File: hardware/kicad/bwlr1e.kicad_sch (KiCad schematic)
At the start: 62 parts, among them J1 Qwiic, Q1 AO3407, Q2 DMG1012UW, SW3 RESET, SW4 BOOT, U1 BME688, U2 RAK3172, U3 AEM10941-QFN, U4 XC6215

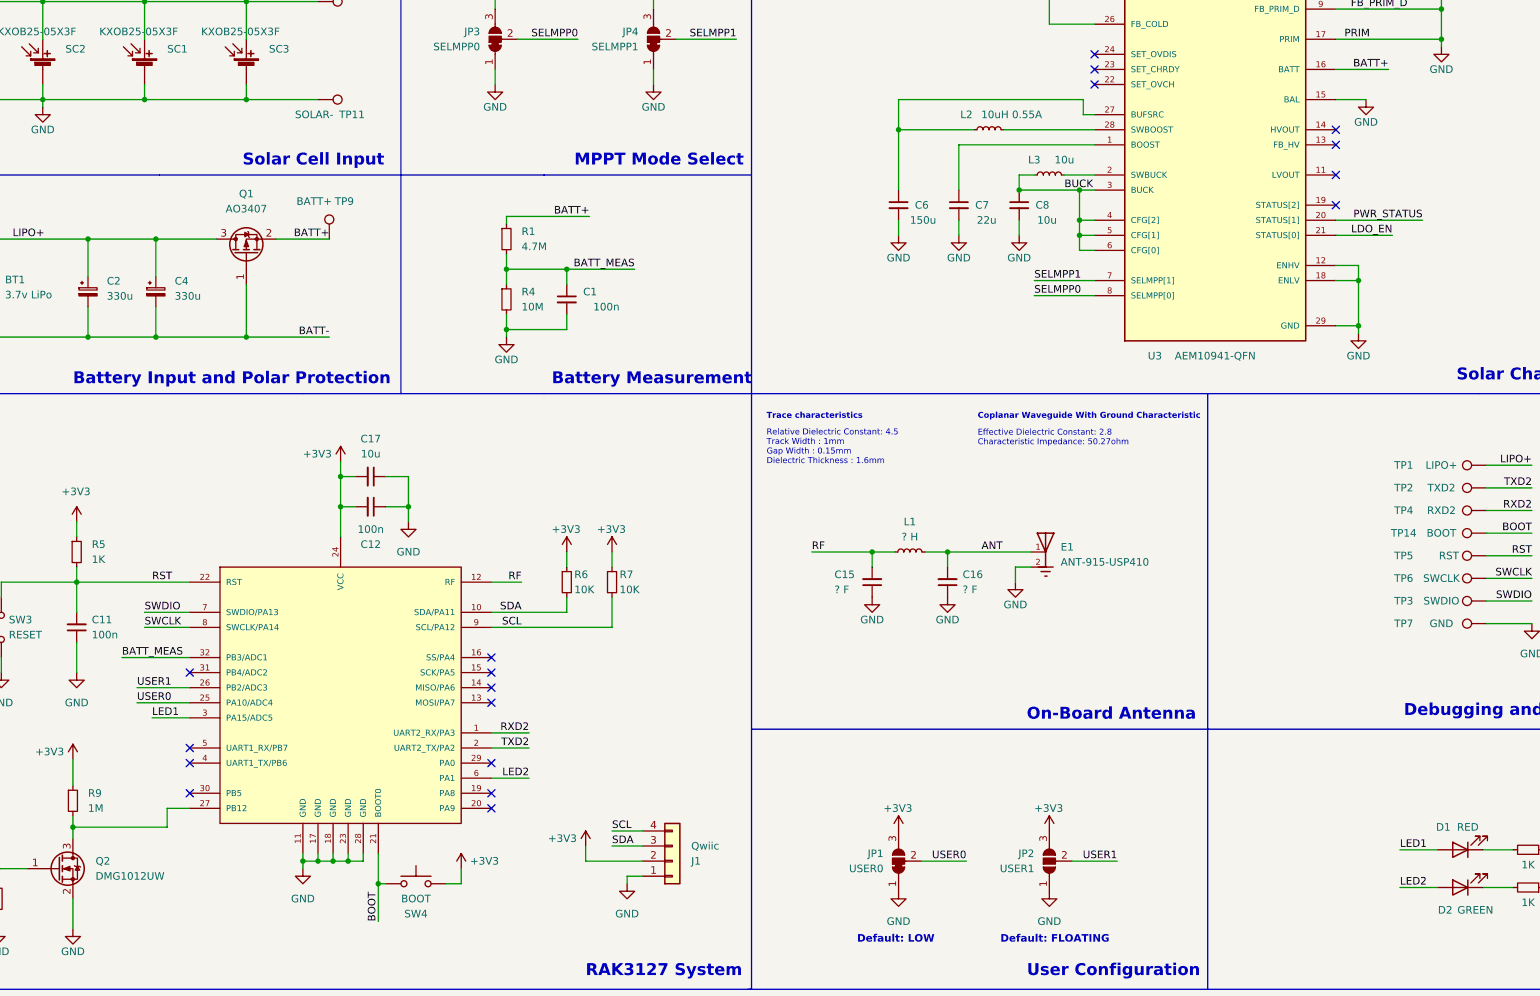
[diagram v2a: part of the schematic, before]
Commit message: small improvement and add production info
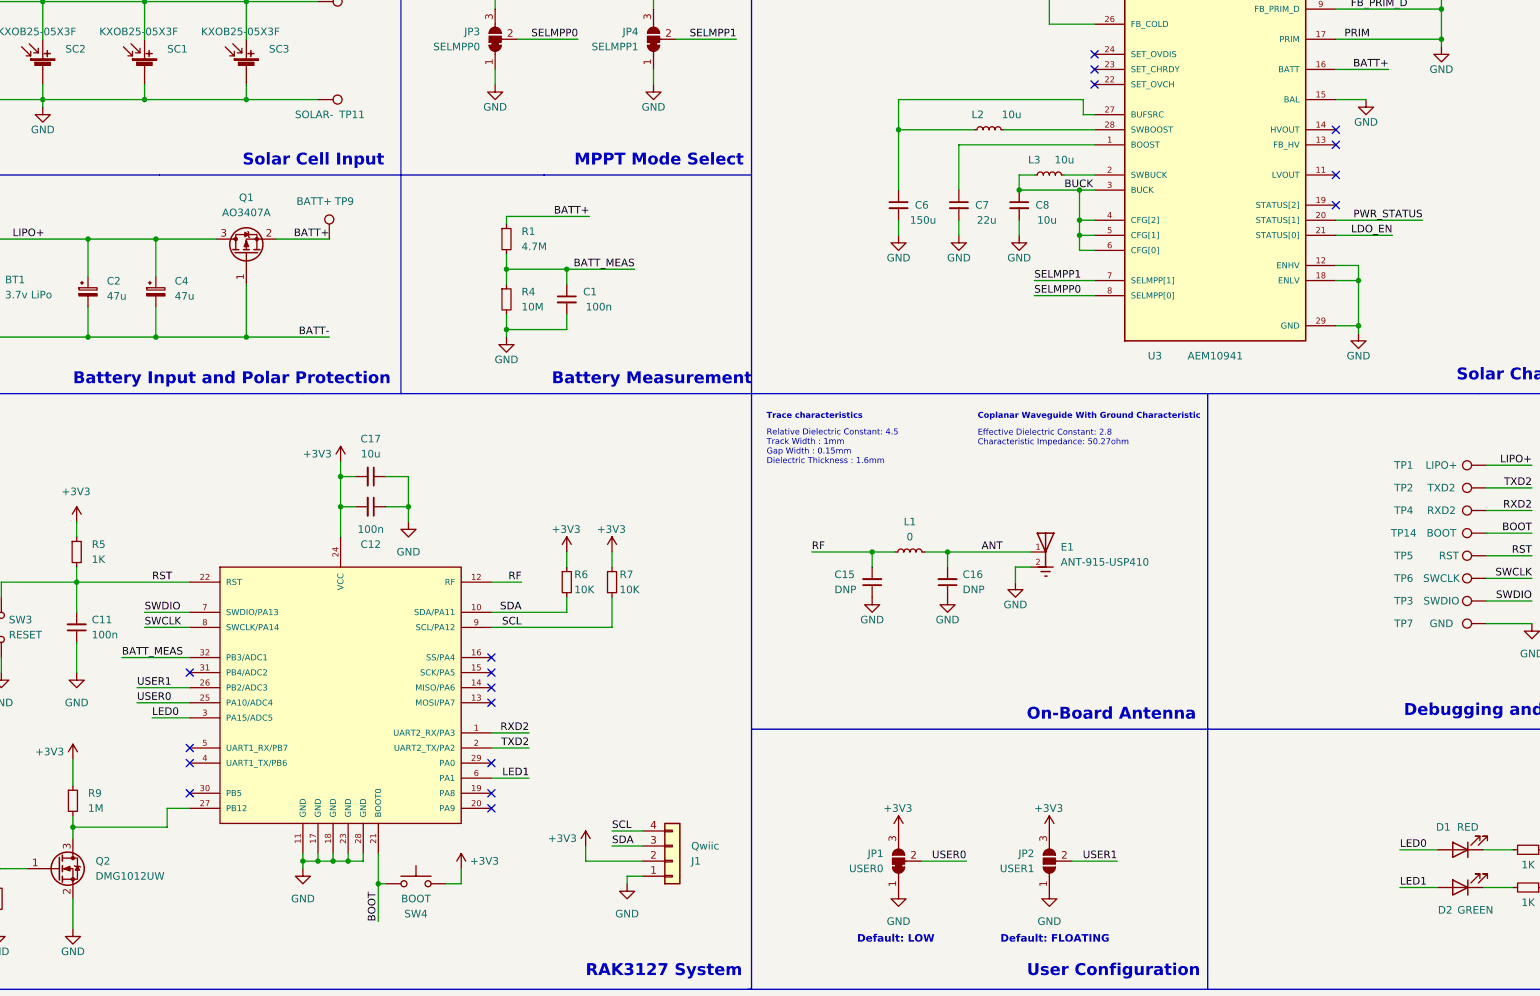
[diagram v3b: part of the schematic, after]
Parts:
- BT1: Manufacturer (none) -> JST; Part Number (none) -> S2B-PH-SM4-TB
- C1, C11, C12, C3, C5: Part Description (none) -> Ceramic Capacitor 100nF 10% 10V X7R
- C13, C14, C8: Mouser https://www.mouser.com/ProductDetail/Murata-Electronics/GRM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 -> (none); Part Description (none) -> Ceramic Capacitor 10uF 10% 10V X5R
- C15, C16: value ? F -> DNP
- C17: Part Description (none) -> Ceramic Capacitor 10uF 10% 10V X5R
- C2, C4: value 330u -> 47u; Manufacturer (none) -> KYOCERA AVX; Part Number (none) -> TPSB476K010R0350
- C6: Mouser https://www.mouser.com/ProductDetail/Murata-Electronics/GRM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 -> (none); Part Description (none) -> Ceramic Capacitor 150uF 20% 6.3V X5R
- C7: Mouser https://www.mouser.com/ProductDetail/Murata-Electronics/GRM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 -> (none); Part Description (none) -> Ceramic Capacitor 22uF 20% 10V X5R
- D1: Part Description (none) -> Red 2V 20mA
- D2: Part Description (none) -> Green 2V 20mA
- E1: Manufacturer (none) -> Linx Technologies Inc.; Part Number (none) -> ANT-915-USP410
- J1: Manufacturer (none) -> JST Sales America; Part Number (none) -> SM04B-SRSS-TB
- L1: value ? H -> 0
- L2: value 10uH 0.55A -> 10u; Mouser https://www.mouser.com/ProductDetail/Coilcraft/LPS4012-103M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 -> (none); Part Description (none) -> Power Inductor 10uH 20% 1.1A
- L3: Mouser https://www.mouser.com/ProductDetail/TDK/MLZ1608M100WT000?q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 -> (none); Part Description (none) -> Power Inductor 10uH 20% 90mA
- Q1: value AO3407 -> AO3407A; Manufacturer (none) -> Alpha & Omega Semicon; Part Number (none) -> AO3407A
- Q2: Manufacturer (none) -> TECH PUBLIC; Part Number (none) -> DMG1012UW
- R1: Part Description (none) -> Resistor 4.7M 1% 100mW
- R12, R13, R5: Part Description (none) -> Resistor 1K 5% 100mW
- R2, R3, R6, R7: Part Description (none) -> Resistor 10K 5% 100mW
- R4: Part Description (none) -> Resistor 10M 1% 100mW
- R8, R9: Part Description (none) -> Resistor 1M 5% 100mW
- SC1, SC2, SC3, SC4: Manufacturer (none) -> ANYSOLAR Ltd; Part Number (none) -> KXOB25-05X3F
- SW3, SW4: Manufacturer (none) -> E-Switch; Part Number (none) -> TL3342F160QG
- U1: Manufacturer (none) -> Bosch Sensortec; Part Number (none) -> BME688
- U2: value RAK3172 -> RAK3172-T; Manufacturer (none) -> RAKwireless; Part Description (none) -> RAK3172-T Module with TCXO without IPEX 915MHz AS923; Part Number (none) -> 309054
- U3: value AEM10941-QFN -> AEM10941; MANUFACTURER e-peas semiconductors -> (none); MAXIMUM_PACKAGE_HEIGHT 0.9 mm -> (none); Manufacturer (none) -> e-peas; PARTREV 1.4 -> (none); Part Number (none) -> AEM10941-QFN; STANDARD IPC-7351B -> (none)
- U4: Manufacturer (none) -> Torex Semicon; Part Number (none) -> XC6215B332MR-G
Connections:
- net LED2 is gone; now on net LED1: D2.2 (A), U2.6 (PA1)
- net LED1: no longer D1.2 (A), U2.3 (PA15/ADC5)
- new net LED0: D1.2 (A), U2.3 (PA15/ADC5)

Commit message: update RAK3172 description
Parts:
- U2: Part Description RAK3172-T Module with TCXO without IPEX 915MHz AS923 -> RAK3172-T Module with TCXO, without IPEX, Frequency 915MHz,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
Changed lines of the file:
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@@
       (effects (font (size 1.27 1.27)) hide)
     )
-    (property "Part Description" "RAK3172-T Module with TCXO without IPEX 915MHz AS923 " (at 92.71 138.43 0)
+    (property "Part Description" "RAK3172-T Module with TCXO, without IPEX, Frequency 915MHz, Band AS923 " (at 92.71 138.43 0)
       (effects (font (size 1.27 1.27)) hide)
     )
